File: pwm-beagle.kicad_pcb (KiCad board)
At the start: 4 copper layers, 54.6 x 86.4 mm, 60 parts, among them J1 UART, J12 TSENSOR2, J17 FAN_POWER2, J18 FAN_OUT_D1, J19 FAN_OUT_D2, J2 FAN_OUT_A1, J20 FAN_OUT_D3, J21 FAN_OUT_D4, J22 TSENSOR3, J23 TSENSOR4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

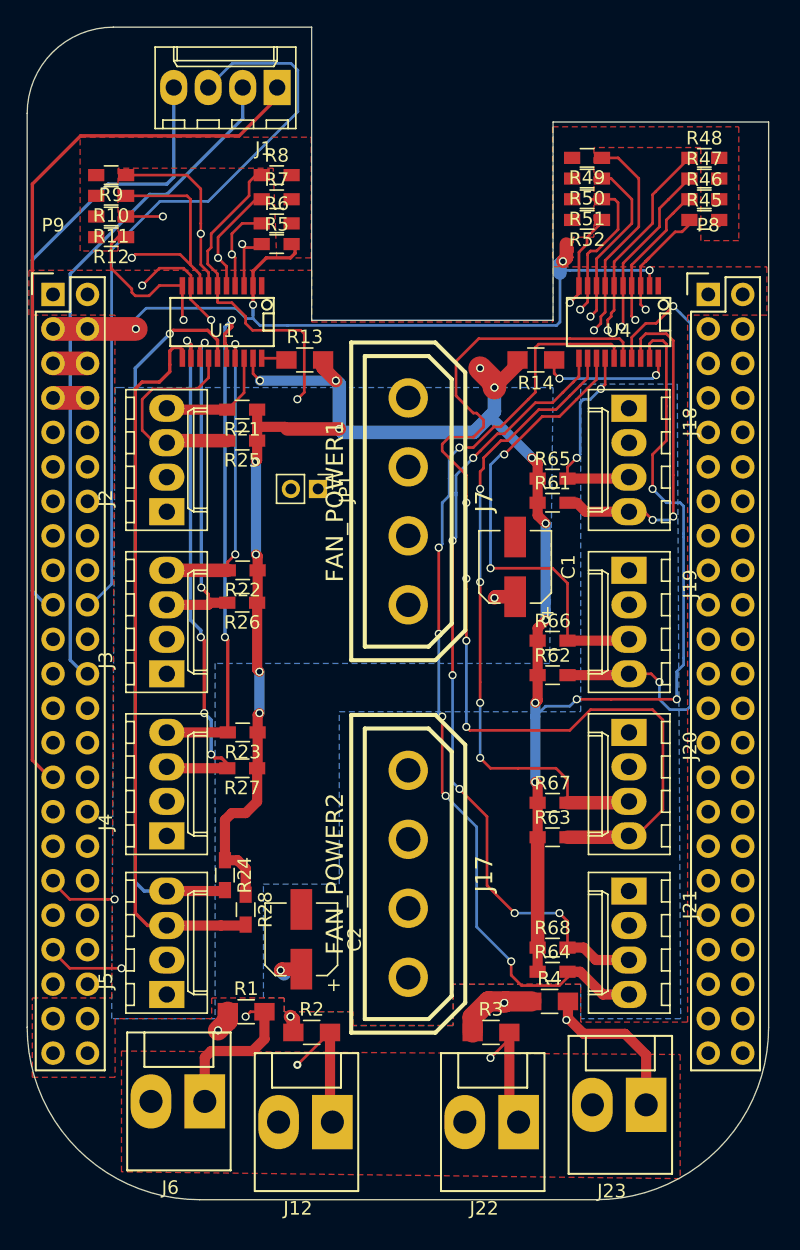
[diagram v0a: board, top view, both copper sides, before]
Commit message: Move silkscreen labels around for clarity
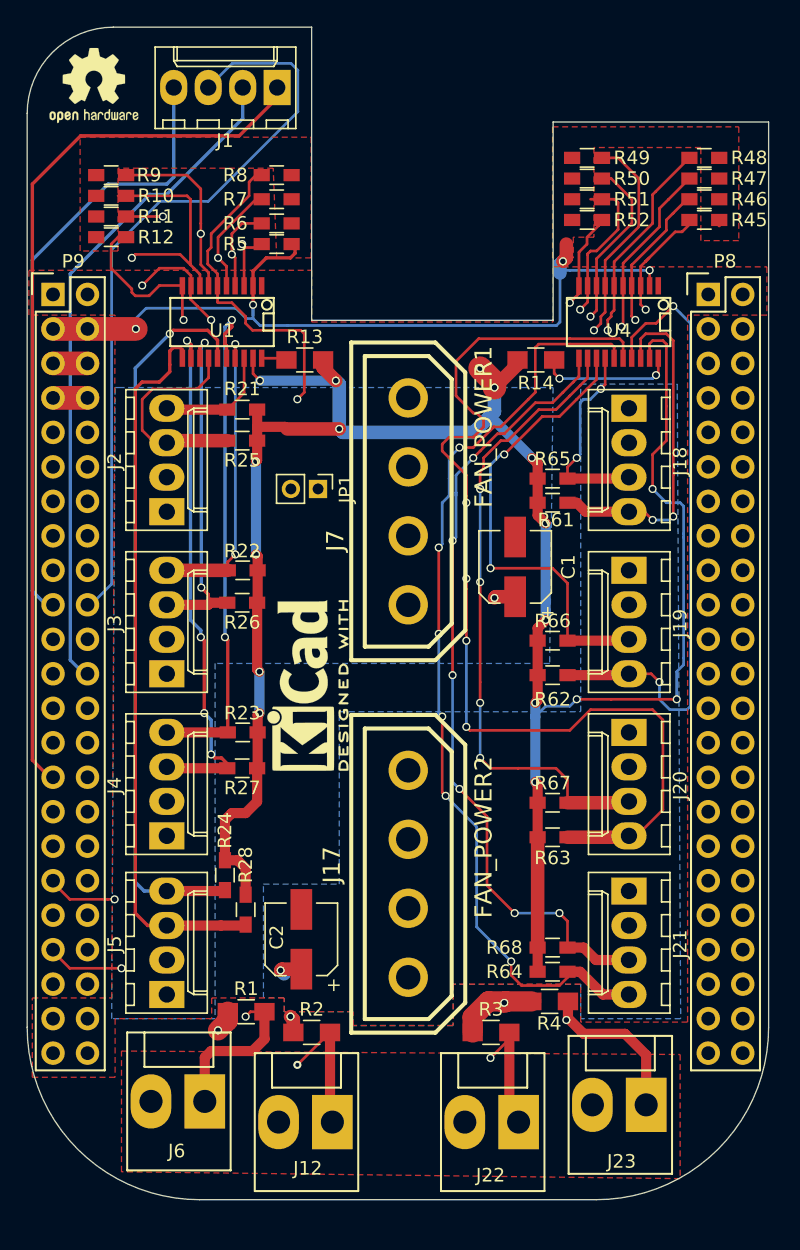
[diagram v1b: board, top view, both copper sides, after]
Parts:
- added ?: , Symbols:OSHW-Logo2_7.3x6mm_SilkScreen, F.Cu at (119.4, 47.0)
- added ?: , Symbols:KiCad-Logo2_6mm_SilkScreen, F.Cu at (135.1, 91.2)
